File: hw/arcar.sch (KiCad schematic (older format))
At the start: 53 parts, among them J1 USB_B_Micro, J2 MOTOR, J3 POWER, M1 screw, M2 screw, P1 AVR_ISP_02X03, SW1 SW_Push, U1 USBLC6-2SC6, U2 ATMEGA328PB-AU, U3 CP2102, U4 ULN2003A, U5 LSM9DS1, U6 TLE52062GAUMA1, U7 RN4871, U8 MCP1804T-3302I/DB

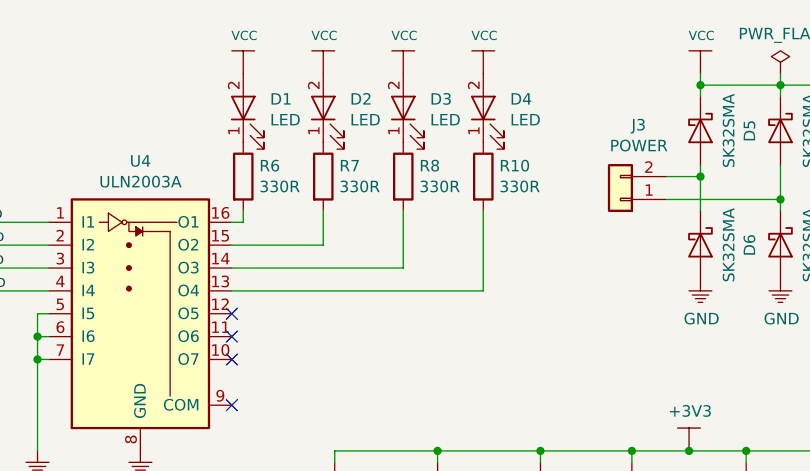
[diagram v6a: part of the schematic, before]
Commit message: change LED resistors
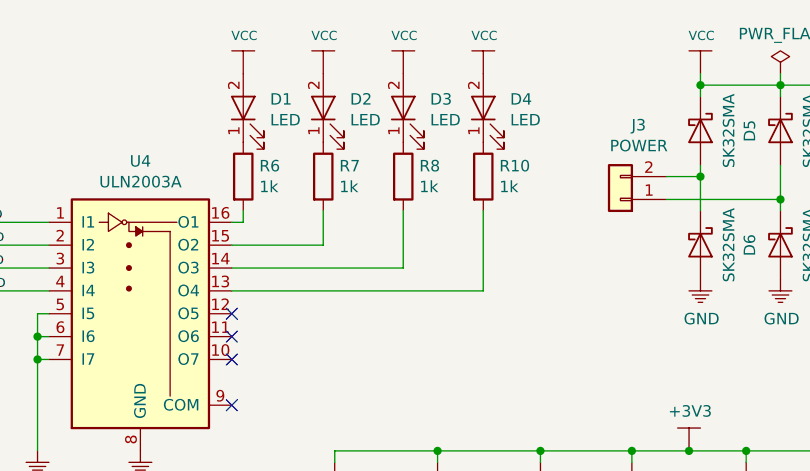
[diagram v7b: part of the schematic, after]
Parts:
- R10, R6, R7, R8: value 330R -> 1k
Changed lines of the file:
@@
 P 5950 1500
 F 0 "R6" H 6020 1546 50  0000 L CNN
-F 1 "330R" H 6020 1455 50  0000 L CNN
+F 1 "1k" H 6020 1455 50  0000 L CNN
 F 2 "Resistors_SMD:R_0805_HandSoldering" V 5880 1500 50  0001 C CNN
 F 3 "" H 5950 1500 50  0001 C CNN
@@
 P 6300 1500
 F 0 "R7" H 6370 1546 50  0000 L CNN
-F 1 "330R" H 6370 1455 50  0000 L CNN
+F 1 "1k" H 6370 1455 50  0000 L CNN
 F 2 "Resistors_SMD:R_0805_HandSoldering" V 6230 1500 50  0001 C CNN
 F 3 "" H 6300 1500 50  0001 C CNN
@@
 P 6650 1500
 F 0 "R8" H 6720 1546 50  0000 L CNN
-F 1 "330R" H 6720 1455 50  0000 L CNN
+F 1 "1k" H 6720 1455 50  0000 L CNN
 F 2 "Resistors_SMD:R_0805_HandSoldering" V 6580 1500 50  0001 C CNN
 F 3 "" H 6650 1500 50  0001 C CNN
@@
 P 7000 1500
 F 0 "R10" H 7070 1546 50  0000 L CNN
-F 1 "330R" H 7070 1455 50  0000 L CNN
+F 1 "1k" H 7070 1455 50  0000 L CNN
 F 2 "Resistors_SMD:R_0805_HandSoldering" V 6930 1500 50  0001 C CNN
 F 3 "" H 7000 1500 50  0001 C CNN
